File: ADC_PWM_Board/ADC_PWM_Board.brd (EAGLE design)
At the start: 57 x 41 mm, 52 parts, among them J1 22-05-7028-02, J10 22-05-7028-02, J11 22-05-7038-03, J2 22-05-7028-02, J3 22-05-7048-04, J4 22-05-7048-04, J5 22-05-7048-04, J6 22-05-7038-03, J7 22-05-7048-04, J8 22-05-7058-05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

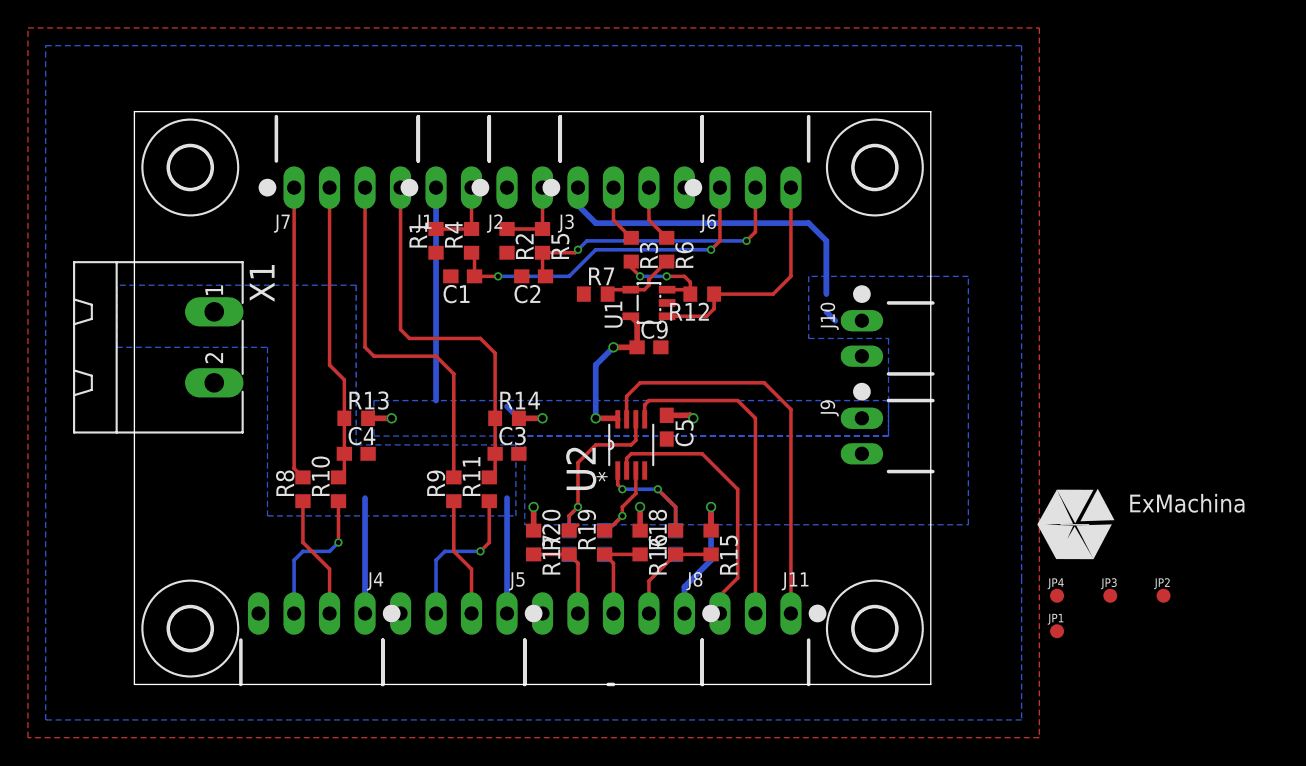
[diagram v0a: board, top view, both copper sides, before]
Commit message: Add opto to the Fan sensor and finsh to route it
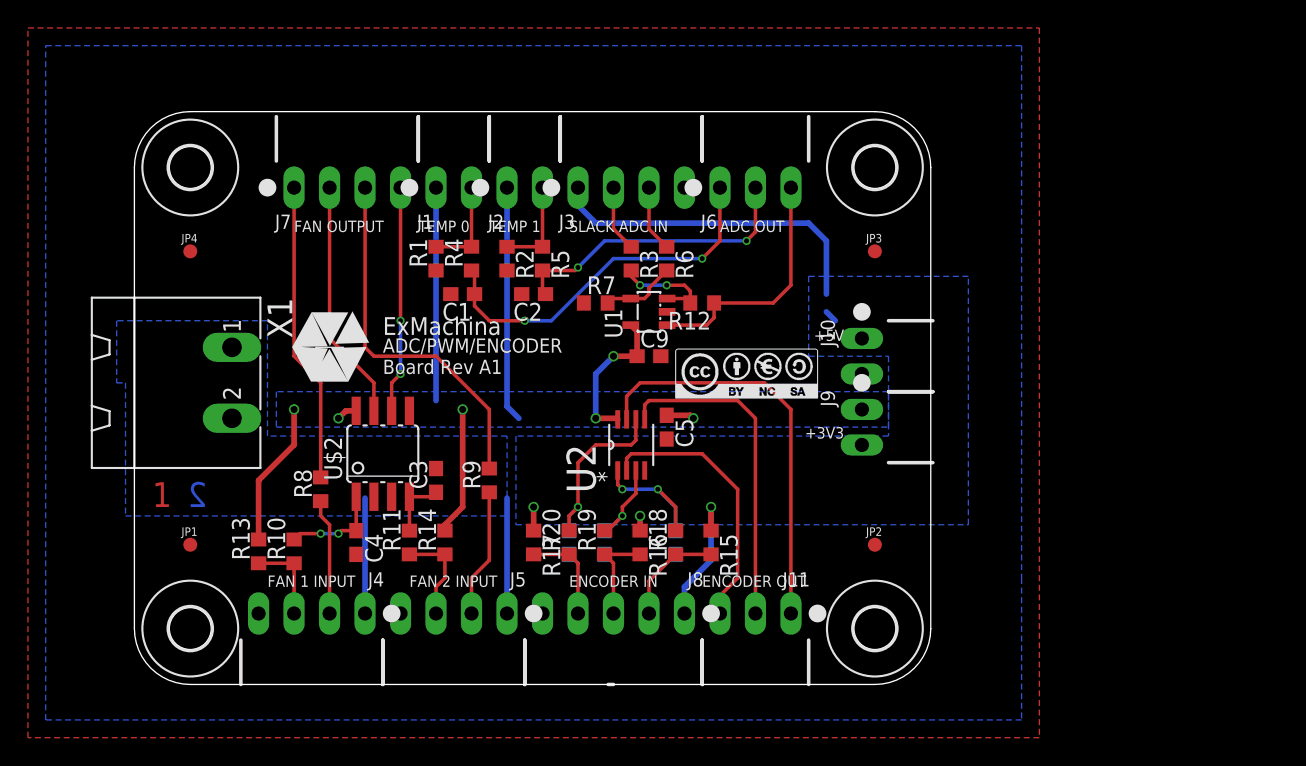
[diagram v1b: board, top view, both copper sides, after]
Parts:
- added U$1: CC-BY-NC-SA, cc-by-sa:CC-BY-NC-SA
- added U$2: HCPL0631, optocoupler:SOIC08
- C1, C2, C3, C4: value 4.7uF -> 0.1uF
- R13, R14, R4, R5: value 10K -> 1K
- moved JP4 66.8 mm to (4.00, 31.0)
- moved JP1 62.3 mm to (4.00, 10.0)
- moved T1 54.8 mm to (14.0, 24.1)
- moved JP3 29.9 mm to (53.0, 31.0)
- moved JP2 21.0 mm to (53.0, 10.0)
- moved R13 11.8 mm to (8.89, 9.53), turned to 90 degrees
- moved R14 9.94 mm to (22.2, 10.2), turned to 90 degrees
- moved R11 6.87 mm to (19.7, 10.2)
- moved C4 6.35 mm to (15.9, 10.2), turned to 270 degrees
- moved R10 5.46 mm to (11.4, 9.53)
- moved C3 5.43 mm to (21.6, 14.6), turned to 90 degrees
- moved X1 2.84 mm to (1.91, 21.6)
- moved R9 2.62 mm to (25.4, 14.6)
- moved R8 1.27 mm to (13.3, 14.0)
- moved C1 1.27 mm to (23.5, 27.9)
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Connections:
- removed net N$12: J5.3, R11.1
- removed net N$14: J4.3, R10.1
- new net N$1: J4.3, R10.1, R13.1
- new net N$2: J5.3, R11.1, R14.1
- new net N$3: C4.1, R10.2, U$2.1
- new net N$4: C3.1, R11.2, U$2.4
- net +3V3: now also U$2.8
- net FAN_1_SENSOR: now also U$2.7; no longer C4.1, R10.2, R13.1
- net FAN_2_SENSOR: now also U$2.6; no longer C3.1, R11.2, R14.1
- net GND: now also U$2.2, U$2.3, U$2.5
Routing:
- net +3V3: track 33.1 -> 65.8 mm, vias 5 -> 6
- net N$12: track 11.1 -> 0.00 mm, vias 1 -> 0
- net N$14: track 10.5 -> 0.00 mm, vias 1 -> 0
- net FAN_2_SENSOR: track 26.7 -> 16.2 mm, vias 0 -> 2
- net N$3: track 0.00 -> 7.13 mm, vias 0 -> 2
- net N$2: track 0.00 -> 7.03 mm
- net N$1: track 0.00 -> 6.13 mm
- net N$4: track 0.00 -> 4.46 mm
- net FAN_1_SENSOR: track 21.4 -> 17.3 mm
- net ADC_TEMP_0: track 24.2 -> 26.8 mm
- net N$66: track 5.50 -> 6.77 mm
- net N$65: track 5.50 -> 6.77 mm
- net N$52: track 14.1 -> 13.4 mm
- net ADC_SLACK_DETECTION: track 17.0 -> 17.6 mm
- net +5V: track 38.3 -> 37.7 mm
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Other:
- outline, holes or cut-outs redrawn
- board text added: "+3V3"
- board text added: "+5V"
- board text added: "1"
- board text added: "2"
- board text added: "ADC OUT"
- board text added: "ADC/PWM/ENCODER Board Rev A1"
- board text added: "ENCODER IN"
- board text added: "ENCODER OUT"
- board text added: "FAN 1 INPUT"
- board text added: "FAN 2 INPUT"
- board text added: "FAN OUTPUT"
- board text added: "SLACK ADC IN"
- board text added: "TEMP 0"
- board text added: "TEMP 1"

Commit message: Replacing name and value on the board
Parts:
- removed U$2: HCPL0631, optocoupler:SOIC08
- removed X1: MSTBA2, con-phoenix-508:MSTBA2
- added C10: 0.1uF, rcl:C0603
- added J12: 22-05-7038-03, con-molex:7395-03
- added U3: SN74LVC3G17DCTR, ti:SOP65P400X130-8N
- J11: value 22-05-7038-03 -> MSTBA2; device con-molex:7395-03 -> con-phoenix-508:MSTBA2
- J7: value 22-05-7048-04 -> 22-05-7058-05; device con-molex:7395-04 -> con-molex:7395-05
- J8: value 22-05-7058-05 -> 22-05-7048-04; device con-molex:7395-05 -> con-molex:7395-04
- R10: value 100 -> 1K2
- R11: value 100 -> 1K
- R12: value 1K2 -> 1K
- R13, R14: value 1K -> 100
- U2: value SN74LVC3G17DCTR -> HCPL0631; device ti:SOP65P400X130-8N -> optocoupler:SOIC08
- moved J11 45.6 mm to (1.91, 21.6), turned to 270 degrees
- moved J7 35.9 mm to (34.3, 5.08), turned to 0 degrees
- moved J8 35.9 mm to (15.2, 35.6), turned to 180 degrees
- moved R10 34.2 mm to (40.6, 27.3), turned to 180 degrees
- moved C6 25.6 mm to (14.0, 16.5), flipped to the top
- moved R12 25.2 mm to (22.2, 10.2), turned to 90 degrees
- moved U2 17.8 mm to (17.8, 16.5), turned to 0 degrees
- moved C3 16.9 mm to (38.1, 18.4), turned to 270 degrees
- moved C5 16.9 mm to (21.6, 14.6), turned to 90 degrees
- moved C9 14.5 mm to (31.1, 10.2), flipped to the bottom, turned to 270 degrees
- moved R11 10.8 mm to (8.89, 9.53)
- moved C7 5.08 mm to (38.7, 10.2)
- moved C8 2.54 mm to (33.7, 10.2)
- moved R14 2.54 mm to (19.7, 10.2)
- moved R13 2.54 mm to (11.4, 9.53)
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- renumbered U$1 to CC1
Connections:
- net +24V: now also J11.1; no longer X1.1
- net +3V3: now also C10.1, C3.1, C6.1, R11.2, R12.2, U3.8; no longer C5.1, C9.1, R13.2, R14.2, U$2.8
- net +5V: now also J7.1; no longer J8.1
- net ADC_SLACK_DETECTION: now also R10.1; no longer R12.1
- net ENCODER_A: now also J12.1, U3.7; no longer J11.1, U2.7
- net ENCODER_B: now also J12.2, U3.5; no longer J11.2, U2.5
- net ENCODER_Z: now also J12.3, U3.2; no longer J11.3, U2.2
- net FAN_1_PWM: now also J8.1; no longer J7.1
- net FAN_1_SENSOR: now also J8.2, U2.7; no longer J7.2, U$2.7
- net FAN_2_PWM: now also J8.3; no longer J7.3
- net FAN_2_SENSOR: now also J8.4, U2.6; no longer J7.4, U$2.6
- net GND: now also C10.2, J11.2, J7.5, U2.2, U2.3, U2.5, U3.4; no longer J8.5, U$2.2, U$2.3, U$2.5, U2.4, X1.2
- net N$1: now also R11.1; no longer R10.1
- net N$2: now also R12.1; no longer R11.1
- net N$3: now also R13.2, U2.1; no longer R10.2, U$2.1
- net N$35: now also J7.2; no longer J8.2
- net N$4: now also C5.1, R14.2, U2.4; no longer C3.1, R11.2, U$2.4
- net N$40: now also J7.3; no longer J8.3
- net N$46: now also J7.4; no longer J8.4
- net N$52: now also C9.1, U3.6; no longer C8.1, U2.6
- net N$53: now also C8.1, U3.3; no longer C7.1, U2.3
- net N$54: now also C7.1, U3.1; no longer C6.1, U2.1
- net N$61: now also R10.2; no longer R12.2
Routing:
- net N$11: track 8.30 -> 9.59 mm
- net +3V3: track 65.8 -> 67.1 mm, vias 6 -> 7
- net +5V: track 37.7 -> 38.6 mm
- net FAN_1_PWM: track 21.5 -> 20.7 mm

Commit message: Rename fabrication folder
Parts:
- J10: value 22-05-7028-02 -> MSTBA2; device con-molex:7395-02 -> con-phoenix-508:MSTBA2
- J11: value MSTBA2 -> 22-05-7038-03; device con-phoenix-508:MSTBA2 -> con-molex:7395-03
- R15, R16, R17: value 4K7 -> 2K7
- moved J11 50.4 mm to (52.1, 17.1), turned to 90 degrees
- moved J10 50.2 mm to (1.91, 21.6), turned to 270 degrees
- moved J9 5.08 mm to (52.1, 23.5)
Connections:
- new net AVDD: J1.1, J11.1, J2.1
- net +24V: now also J10.1; no longer J11.1
- net +3V3: now also J11.2; no longer J1.1, J2.1, J9.1
- net +5V: now also J7.4, J9.1; no longer J10.1, J7.1
- net GND: now also J11.3, J7.1; no longer J11.2, J7.5
- net N$35: now also J7.3; no longer J7.2
- net N$40: now also J7.5; no longer J7.3
- net N$46: now also J7.2; no longer J7.4
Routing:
- net AVDD: track 0.00 -> 52.6 mm
- net +3V3: track 67.1 -> 35.0 mm
- net N$46: track 7.03 -> 11.7 mm
- net N$35: track 7.56 -> 10.5 mm, vias 0 -> 1
- net N$40: track 7.03 -> 9.85 mm, vias 0 -> 2
